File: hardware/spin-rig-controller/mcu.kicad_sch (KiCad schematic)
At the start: 51 parts, among them J201 USB4110GFA, J202 PI, J203 QWIIC, SW201 BOOT, SW202 RESET, U201 ESP32-S3FN8, Y201 40 MHz

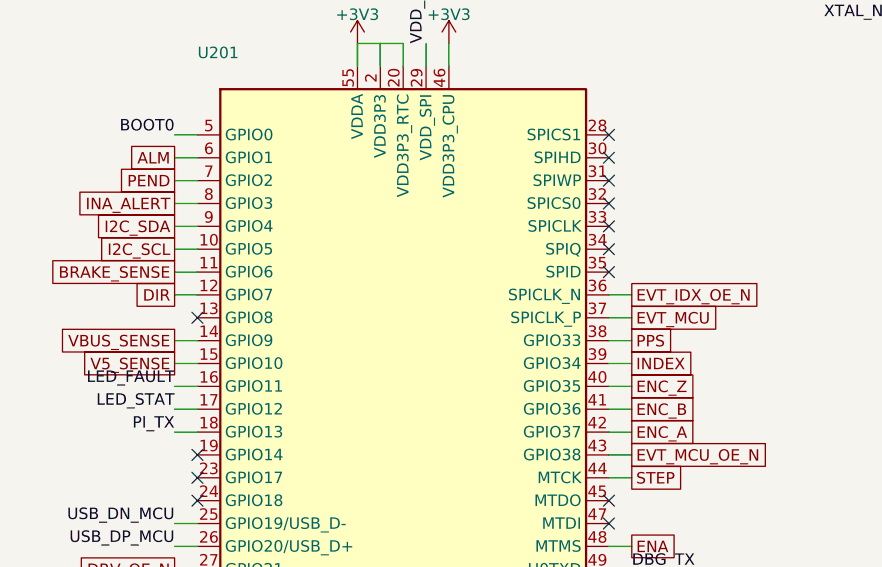
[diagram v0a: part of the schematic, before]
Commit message: hardware(spin-rig-controller): the driver's own plugs -- XT60 pack input, CL57T 3.5 mm headers in its pin order, and an encoder pass-through
After the first review, the connectors change so the assembly plugs together instead of being wired up:
- J101 is an XT60PW-M (right angle, top edge), matching the rig's pack and anti-spark switch;
- J103 (driver feed), J301 (control) and the new J305 (encoder out) are 3.5 mm Phoenix MC headers that take
  the CL57T's own pluggable plugs, in its order: P4 +VDC GND; P1 PUL+ PUL- DIR+ DIR- ENA+ ENA- ALM BRK COM-;
  P2 EB+ EB- EA+ EA- VCC EGND. The silkscreen names every pin;
- the motor's encoder extension lead lands on J302 (right edge) and passes through to J305; the AM26LV32E
  reads A and B on the way. J302 is numbered from the bottom so the six traces nest around the corner;
- J303, J304 and J104 become through-hole JST PH. J102 (brake resistor) is now the only VH connector, which
  ends the three look-alike power connectors.

The CL57T V4.x has no in-position output: its ALM and BRK are open-collector to a shared COM- (CL57T V4.0
manual, CL42T/CL86T V4.1 manuals). The input that read PEND now reads BRK (DRV_BRK, GPIO2), and ENC_Z is
dropped (the encoder has no index; GPIO35 is free). The Qwiic connector moves beside the INA238.

Through-hole parts (design.HAND) are out of the JLC BOM and CPL; make_fab.py lists them in -hand.csv
(29 extended part types now, about $23 of JLC parts a board). The router's leftovers are closed by
gen/hand_fixes.py, planned against the copper around each (gen/region.py lists a window's copper).
ERC 0 errors (the shared SP0503 symbol's 4 warnings); DRC 0 errors, 0 unconnected, schematic parity clean;
tools/check_board_parity.py passes. Still to measure: the CL57T's terminal pitch (3.5 mm assumed). Not ordered.

Co-Authored-By: Claude Opus 5.5 <noreply@anthropic.com>
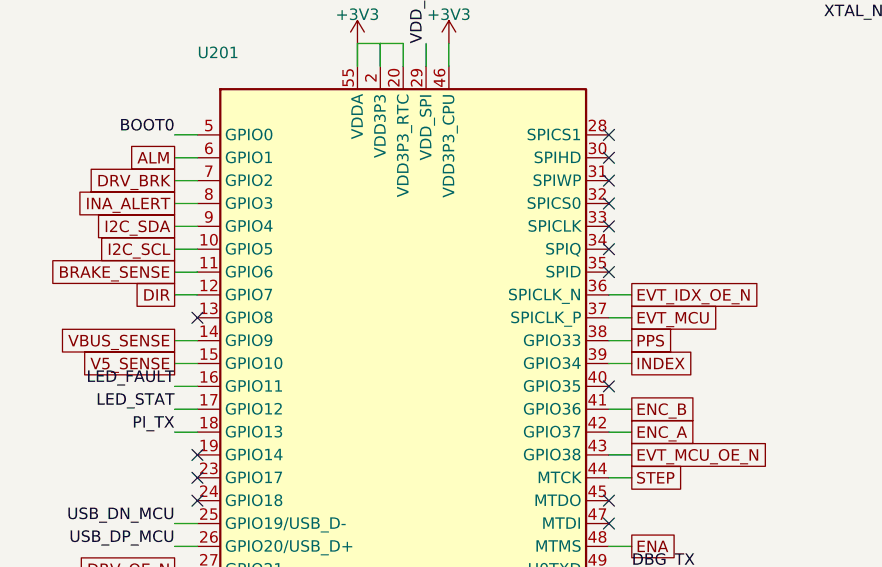
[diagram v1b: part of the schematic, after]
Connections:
- net ENC_Z: no longer names the net of U201.40 (GPIO35)
- net PEND renamed DRV_BRK
- no-connect marks 18 -> 19
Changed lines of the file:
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@@
 		)
 	)
-	(global_label "PEND"
+	(global_label "DRV_BRK"
 		(shape passive)
 		(at 30.48 62.23 180)
@@
 		)
 	)
-	(wire
-		(pts
-			(xy 78.74 85.09)
-			(xy 81.28 85.09)
-		)
-		(stroke
-			(width 0)
-			(type default)
-		)
-	)
-	(global_label "ENC_Z"
-		(shape passive)
-		(at 81.28 85.09 0)
-		(fields_autoplaced yes)
-		(effects
-			(font
-				(size 1.27 1.27)
-			)
-			(justify left)
-		)
-		(property "Intersheetrefs" "${INTERSHEET_REFS}"
-			(at 81.28 85.09 0)
-			(hide yes)
-			(show_name no)
-			(do_not_autoplace no)
-			(effects
-				(font
-					(size 1.27 1.27)
-				)
-				(justify left)
-			)
-		)
-	)
-	(wire
+	(no_connect
+		(at 78.74 85.09)
+	)
+	(wire

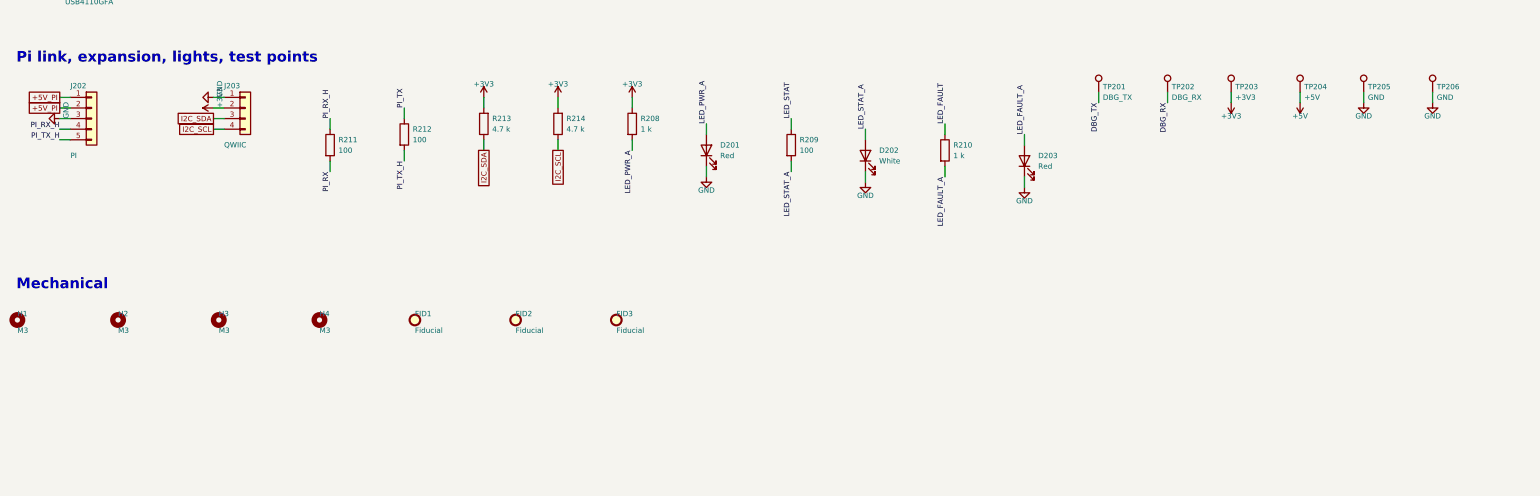
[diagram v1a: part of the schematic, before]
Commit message: hardware(spin-rig-controller): stacks on the Pi 4B like a HAT -- 2x20 socket on the underside, the Pi's M2.5 holes, USB-C flush
- J202 becomes a 2x20 8.5 mm female socket (Hong Cheng HC-PM254-8.5H-2x20PZ, LCSC C22373925) on the underside,
  on the Pi's header: 5 V in on pins 2 and 4 (F103, 4 A, and a 2 mm feed), the Pi's UART0 on 8 and 10, all
  eight grounds; the Pi's 3.3 V and other GPIOs unconnected. Placed from KiCad's RaspberryPi-HAT template.
- The Pi turns 90 degrees under the left half, its USB/Ethernet end past the bottom edge (the HAT's 65 mm line),
  GPIO edge down x = 56: M2.5 holes H3, H5, H6, H7 on its 58 x 49 mm pattern (H3 was the M3 corner hole),
  M2.5 x 11 mm standoffs. Nothing tall of the Pi's sits under the board; this board's through-hole pins over it
  clear its low parts by about 3 mm.
- J201 (USB-C) moves 0.6 mm in, flush with the edge; the BOOT/RESET switches, their lights and the Qwiic
  connector move to make room.
- Re-placed and re-routed; gen/hand_fixes.py is re-planned for this routing (buck BOOT/EN, C104's ground,
  R101's via, J303's feeder, U101's 3.3 V stub). silk.py puts underside parts' fab text on B.Fab and lets a
  header's end-pin labels step outward.

ERC 0 errors (SP0503's 4 warnings); DRC 0 errors, 0 warnings, 0 unconnected, parity clean; the repo parity gate
passes (173 symbols). README "Stacking on the Pi" covers mounting, clearances, power (no ideal diode: don't
power the Pi from its USB-C while stacked) and the rotor-balance change.

Co-Authored-By: Claude Opus 5.5 <noreply@anthropic.com>
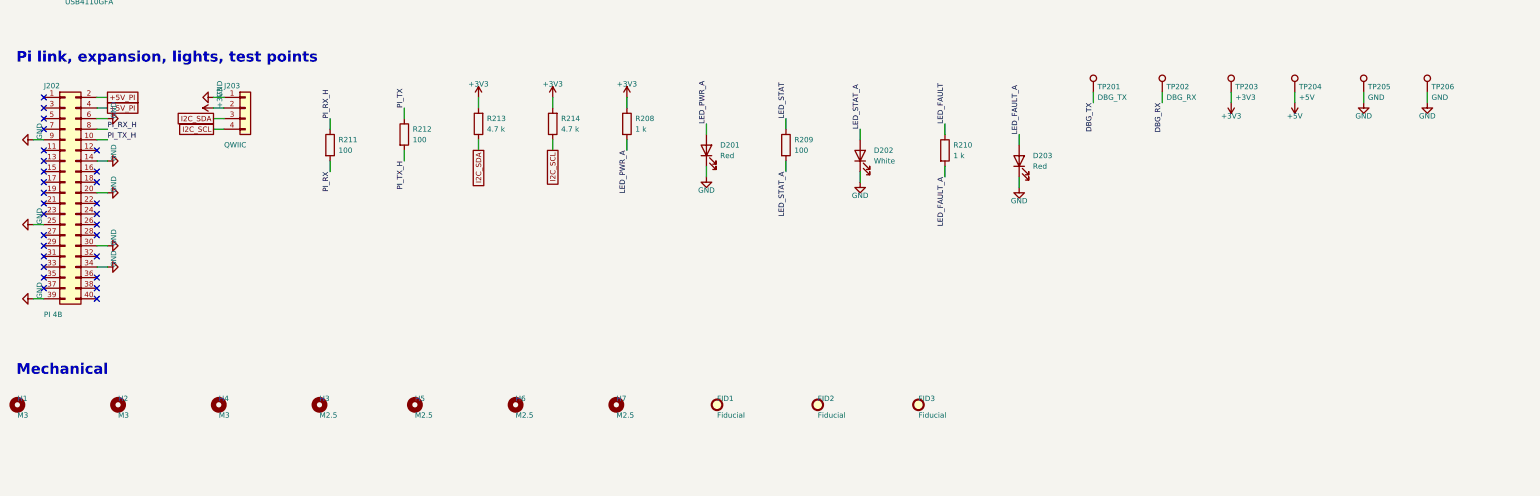
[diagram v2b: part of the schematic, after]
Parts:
- added H5, H6, H7: M2.5, MountingHole:MountingHole_2.7mm_M2.5, symbol Mechanical:MountingHole
- H3: value M3 -> M2.5; footprint MountingHole:MountingHole_3.2mm_M3 -> MountingHole:MountingHole_2.7mm_M2.5
- J202: value PI -> PI 4B; footprint Connector_PinHeader_2.54mm:PinHeader_1x05_P2.54mm_Vertical -> Connector_PinSocket_2.54mm:PinSocket_2x20_P2.54mm_Vertical; symbol Connector_Generic:Conn_01x05 -> Connector_Generic:Conn_02x20_Odd_Even; LCSC C492404 -> C22373925; MPN PZ254V-11-05P -> HC-PM254-8.5H-2x20PZ; Mfr XFCN -> Hong Cheng
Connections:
- net +5V_PI: now also J202.4 (Pin_4); no longer J202.1 (Pin_1)
- net GND: now also J202.14 (Pin_14), J202.20 (Pin_20), J202.25 (Pin_25), J202.30 (Pin_30), J202.34 (Pin_34), J202.39 (Pin_39), J202.6 (Pin_6), J202.9 (Pin_9); no longer J202.3 (Pin_3)
- net PI_RX_H: now also J202.8 (Pin_8); no longer J202.4 (Pin_4)
- net PI_TX_H: now also J202.10 (Pin_10); no longer J202.5 (Pin_5)
- no-connect marks 19 -> 47
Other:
- moved on the sheet: D202, D203, FID1, FID2, FID3, H1, H2, H3, H4, R208, R209, R213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

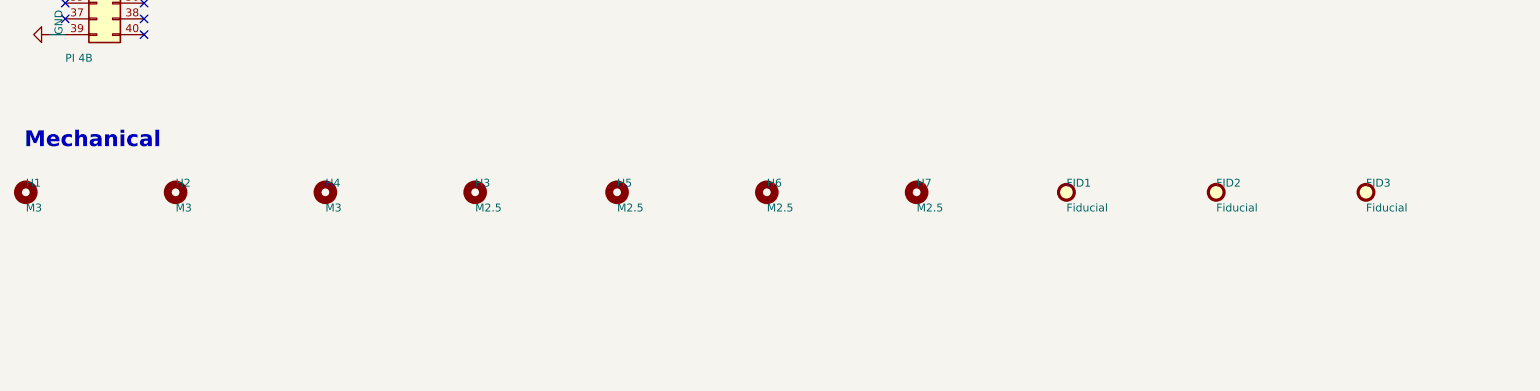
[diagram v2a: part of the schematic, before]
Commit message: hardware(spin-rig-controller): 67 x 90 mm over the Pi 4B -- covers the Pi but its port end, same connectors, one-sided 4-layer
The 110 x 80 board left a lot of empty copper. It now sits over the Pi on the
same 11 mm standoffs and the Pi's four M2.5 holes, with a 25 mm strip at the
top (XT60, input stage, encoder-out) and an 11 mm strip down the right (the
driver headers, index, GNSS) as the only overhang. Every connector and the
encoder pass-through stay; all SMD parts stay on the top side.

- design.py: the three M3 holes and the fiducials dropped (Economic
  assembly doesn't use them).
- make_pcb.py: new placement around U201_XY/U104_XY; the buck's BOOT/RT/EN
  runs and the ESP32's bottom fan-out are now locked pre-routes relative to
  those parts; In2's 5 V plane is the bottom 22 mm; Pi feed re-laid.
- fixup.py: the ESP32's 1.5 mm stitching grid follows U201_XY.
- silk.py: the title shrinks or turns to fit; pin labels and header names
  packed for the right edge.
- hand_fixes.py: re-planned for this routing result.
- README and FABRICATION-NOTES: 67 x 90, 540 vias, new pin-1 table and
  tooling-hole spots.

DRC 0 errors / 0 warnings / 0 unconnected, schematic parity clean, ERC 0
errors (the shared SP0503 symbol's 4 warnings), parity gate 167 symbols.

Co-Authored-By: Claude Opus 5.5 <noreply@anthropic.com>
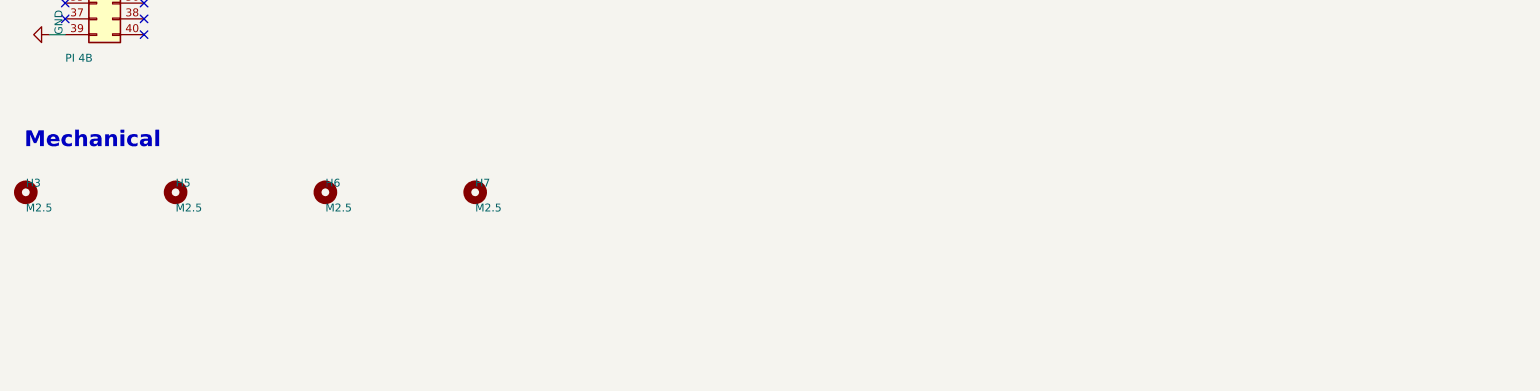
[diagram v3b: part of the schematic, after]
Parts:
- removed FID1, FID2, FID3: Fiducial, Fiducial:Fiducial_1mm_Mask2mm, symbol Mechanical:Fiducial
- removed H1, H2, H4: M3, MountingHole:MountingHole_3.2mm_M3, symbol Mechanical:MountingHole
- TP201, TP202, TP203, TP204, TP205, TP206: footprint TestPoint:TestPoint_Pad_D1.5mm -> TestPoint:TestPoint_Pad_D1.0mm
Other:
- moved on the sheet: H3, H5, H6, H7
